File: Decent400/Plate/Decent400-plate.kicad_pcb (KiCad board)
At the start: 2 copper layers, 252.6 x 93.5 mm, 64 parts, among them SW0 0, SW1 1, SW2 2, SW3 3, SW4 4, SW5 5, SW6 6, SW7 7, SW8 8, SW9 9

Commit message: Decent 400 4i low-profile keyboard with the original 400 layout
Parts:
- removed SWCtl2: Control, Library:MX-1-25U-Hole-no-silk
- SWEsc1: footprint Library:MX-1-25U-Hole-no-silk -> Library:MX-1-00U-Hole-no-silk
- SWLeftSft1: footprint Library:MX-1-25U-Hole-no-silk -> Library:Choc-2U-Hole
- SWRightSft1: footprint Library:Choc-2U-Hole -> Library:MX-1-00U-Hole-no-silk
- moved SWEsc1 88.2 mm to (29.0, 49.0)
- moved SWBrk1 78.6 mm to (265.0, 49.0)
- moved SWTab1 58.5 mm to (34.0, 66.0)
- moved SWCtl1 34.9 mm to (39.0, 83.0)
- moved G*** 25.0 mm to (263.7, 113.6)
- moved REF** 19.9 mm to (254.0, 121.3)
- moved SWInv1 19.6 mm to (240.0, 100.0)
- moved SWDel1 17.4 mm to (248.1, 49.0)
- moved REF** 16.5 mm to (265.0, 120.9)
- moved G*** 13.0 mm to (251.5, 39.0)
- moved SW1 12.6 mm to (45.8, 49.0)
- moved SWQ1 12.2 mm to (56.0, 66.0)
- moved SWA1 11.8 mm to (61.0, 83.0)
- moved SWZ1 11.4 mm to (70.0, 100.0)
- moved SW2 11.3 mm to (62.7, 49.0)
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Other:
- board text added: "Decent 400 rev. 4i © Bertrand Le Roy 2026"
- board text added: "Make as a *1.2mm* PCB for Kailh Choc v1 stabilizer and switch compatibility."
- board text removed: "*"
- board text removed: "+"
- board text removed: ","
- board text removed: "-"
- board text removed: "."
- board text removed: "/"
- board text removed: "0"
- board text removed: "1"
- board text removed: "2"
- board text removed: "3"
- board text removed: "4"
- board text removed: "5"
- board text removed: "6"
- board text removed: "7"
- board text removed: "8"
- board text removed: "9"
- board text removed: ";"
- board text removed: "<"
- board text removed: "="
- board text removed: ">"
- board text removed: "A"
- board text removed: "ATARI"
- board text removed: "B"
- board text removed: "Backlight"
- board text removed: "Break"
- board text removed: "C"
- board text removed: "Caps"
- board text removed: "Control"
- board text removed: "D"
- board text removed: "Decent 400 rev. 3i © Bertrand Le Roy 2023"
- board text removed: "Del"
- board text removed: "E"
- board text removed: "Esc"
- board text removed: "F"
- board text removed: "G"
- board text removed: "H"
- board text removed: "I"
- board text removed: "J"
- board text removed: "K"
- board text removed: "L"
- board text removed: "M"
- board text removed: "Make as a *1.2mm* aluminum PCB for Kailh Choc v1 stabilizer and switch compatibility."
- board text removed: "N"
- board text removed: "O"
- board text removed: "P"
- board text removed: "Q"
- board text removed: "R"
- board text removed: "Return"
- board text removed: "S"
- board text removed: "Shift"
- board text removed: "Space"
- board text removed: "T"
- board text removed: "Tab"
- board text removed: "U"
- board text removed: "V"
- board text removed: "W"
- board text removed: "X"
- board text removed: "Y"
- board text removed: "Z"

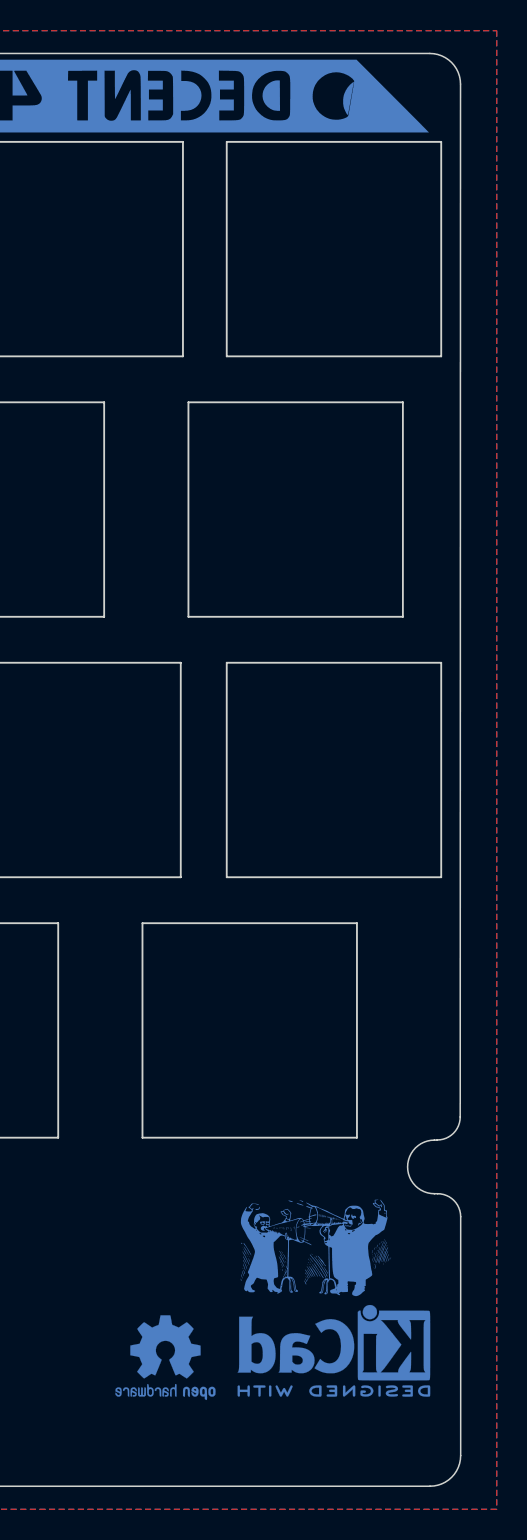
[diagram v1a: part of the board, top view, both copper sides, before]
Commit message: Decent400 rev 4.2i
Moved the luminosity pot left of the right shift key so it's still accessible but not normally visible
Changed the connector to an IDC connector between the main part of the keyboard and the console keys
Fixed alignment issues on console keys
Created all-new cap legends, fake test caps and printed rigs for UV home printing
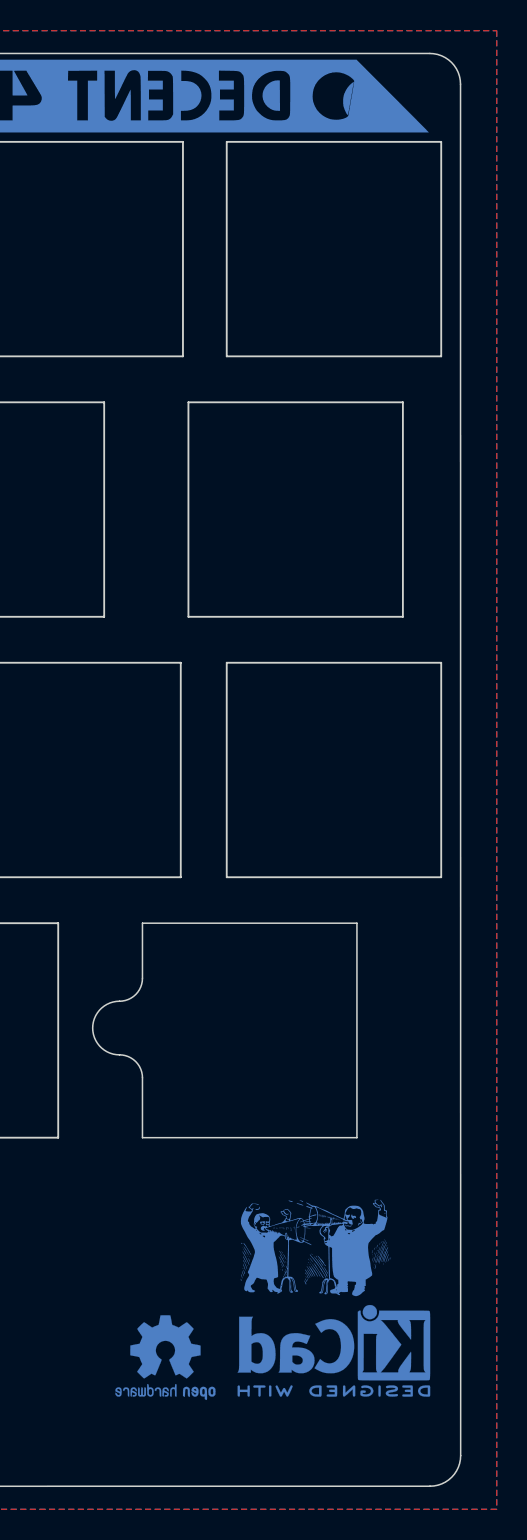
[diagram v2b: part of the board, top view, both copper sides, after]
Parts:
- removed SWRightSft1: Shift, Library:MX-1-00U-Hole-no-silk
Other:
- outline, holes or cut-outs redrawn
- board text added: "Decent 400 rev. 4.2i © Bertrand Le Roy 2026"
- board text removed: "Decent 400 rev. 4i © Bertrand Le Roy 2026"

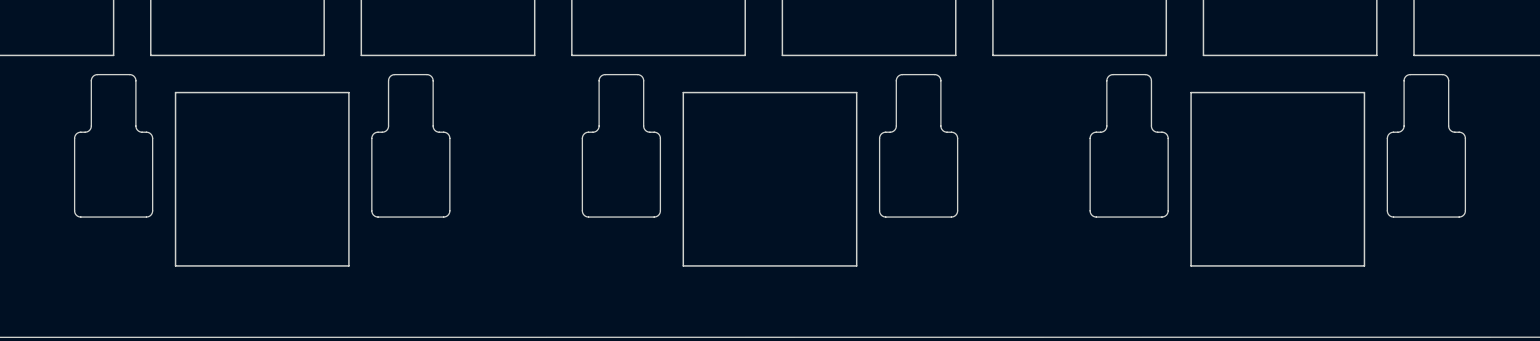
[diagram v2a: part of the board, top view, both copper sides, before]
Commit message: Decent400 rev 4.3i
Change the space bar from 3x2.25U to 1x6.25U
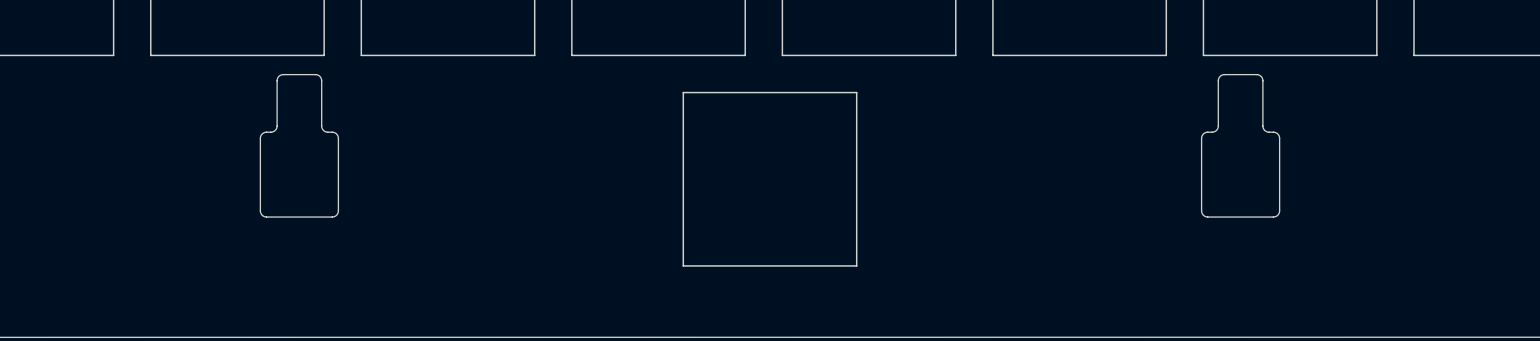
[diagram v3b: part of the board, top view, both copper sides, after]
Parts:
- removed the SWSpc1 at (188.0, 117.0)
- removed the SWSpc1 at (106.0, 117.0)
- SWSpc1: footprint Library:Choc-2U-Hole -> Library:Choc-6.25U-Hole
